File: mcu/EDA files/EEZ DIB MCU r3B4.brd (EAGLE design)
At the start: 139.5 x 70 mm, 201 parts, among them IC1 TPD4E001DRLR, IC10 N.C., IC11 TPS2051BDBVR, IC12 TPS61169DCKR, IC13 TPD4E001DRLR, IC14 TSC2007IPW, IC15 N.C., IC16 DP83848CVV/NOPB, IC2 74AUP1G74DC.125, IC3 CD74HC4050PWR, IC4 STM32F769IIT6, IC5 LD1117ADT33TR, IC6 N.C., IC7 IS42S16400J, IC8 AT24C256C-SSHL-B, IC9 N.C., J1 503398-1892, J2 67803-8020, Q1 N.C., Q2 2N7002, SW1 TL1100CF160Q, SW2 PEC16-2215F-S0024, X1 DS1024-2*20R0, X2 DS1013-16SSIB1, X3 691322110005, X4 N.C., X5 LMJTAB881243M-L, Y1 25MHz, Y2 XTAL016178-85SMX

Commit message: #105
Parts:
- J1: value 503398-1892 -> 5033981892; device EEZ_Lib1:5033981892 -> EEZ_Lib1:5033981892-PCBA
- moved J1 0.60 mm to (49.7, 14.7)
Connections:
- net GND: now also J1.S3
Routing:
- net GND: track 183.0 -> 179.8 mm, vias 320 -> 316
- net LTDC_G6: track 54.6 -> 51.9 mm
- net LTDC_G5: track 31.8 -> 32.3 mm
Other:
- board text added: "EEZ DIB MCU (03/2021 r3B4)"
- board text added: "EEZ DIB MCU (03/2021 r3B4) Project source code: github.com/eez-open/modular-psu"
- board text removed: "EEZ DIB MCU (02/2021 r3B3)"
- board text removed: "EEZ DIB MCU (02/2021 r3B3) Project source code: github.com/eez-open/modular-psu"

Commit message: #88
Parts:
- removed C49: N.C., rcl:C0603
- removed IC10: N.C., EEZ_Lib1:SOT65P210X110-5N
- removed JP7: JP2-NOCUT-0805, EEZ_Lib1:JP2-0805-NOCUT
- added C71: 100n, rcl:C0603
- R12: value N.C. -> 4K7
- moved R12 9.09 mm to (51.4, 65.3), turned to 0 degrees
- moved R4 5.27 mm to (30.1, 11.5)
- moved R8 5.25 mm to (32.7, 11.5)
- moved R22 4.27 mm to (51.4, 67.2)
- moved R25 3.58 mm to (51.4, 63.3)
- moved X3 2.25 mm to (33.8, 6.75)
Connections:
- removed net N$38: R8.2, R9.1
- removed net NRST: IC10.2, IC4.31, JP7.2, R12.2, R25.2
- new net N$60: R4.1, X3.1
- net !RESET: now also C71.2, IC4.31, R12.2, R25.2; no longer IC10.4, JP7.1
- net +3V3: no longer C49.1, IC10.1, IC10.5
- net GND: now also C71.1; no longer C49.2, IC10.3
- net N$41: now also IC1.2, R8.2, R9.1; no longer R4.2, R5.1
- net X_DIN1: now also R4.2, R5.1; no longer R4.1, X3.1
- net X_DIN2: no longer IC1.2
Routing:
- net NRST: track 31.7 -> 0.00 mm
- net !RESET: track 163.5 -> 179.0 mm
- net N$41: track 2.04 -> 9.24 mm, vias 0 -> 2
- net N$60: track 0.00 -> 5.20 mm
- net X_DIN2: track 9.83 -> 4.83 mm, vias 2 -> 0
- net +3V3: track 166.5 -> 163.2 mm, vias 76 -> 75
- net SWD_NRST: track 45.9 -> 48.3 mm
- net N$59: track 5.50 -> 3.18 mm
- net X_DOUT2: track 29.3 -> 31.6 mm
- net X_DOUT1: track 25.9 -> 28.2 mm
- net N$38: track 2.04 -> 0.00 mm
- net X_DIN1: track 12.3 -> 11.7 mm
- net GND: vias 316 -> 315
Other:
- board text added: "EEZ DIB MCU (05/2021 r3B4)"
- board text added: "EEZ DIB MCU (05/2021 r3B4) Project source code: github.com/eez-open/modular-psu"
- board text removed: "EEZ DIB MCU (03/2021 r3B4)"
- board text removed: "EEZ DIB MCU (03/2021 r3B4) Project source code: github.com/eez-open/modular-psu"

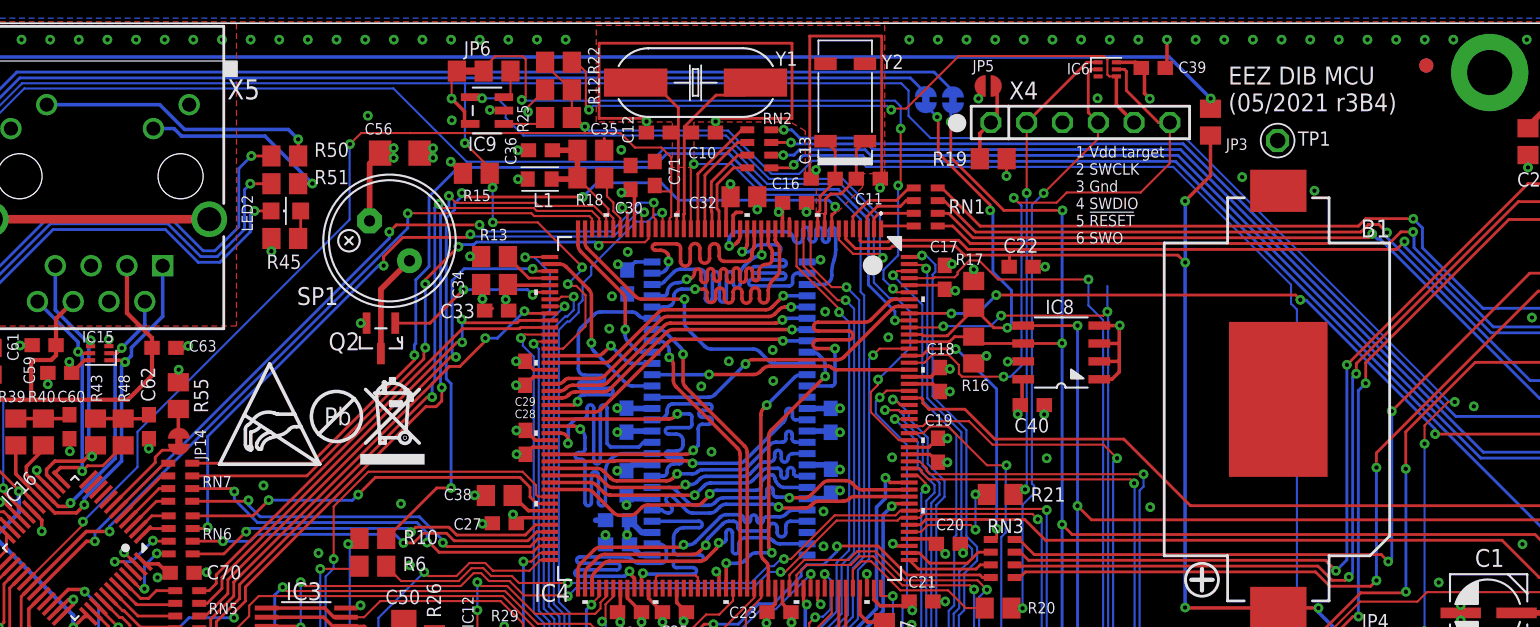
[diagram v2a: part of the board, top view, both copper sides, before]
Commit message: PCB layout for SMD/THT loudspeaker
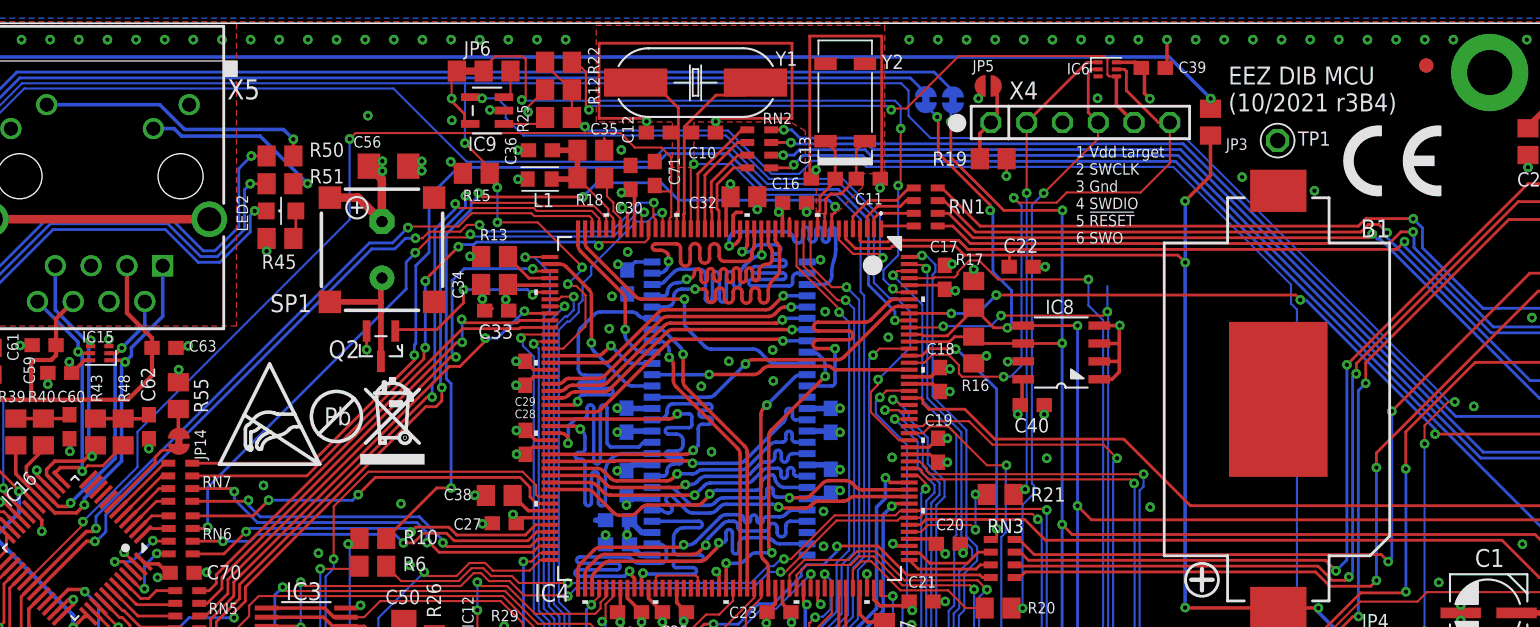
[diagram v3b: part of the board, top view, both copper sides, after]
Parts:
- added U$3: (no value), logo:CE_5MM
- C10, C12: value 33p -> 18p
- SP1: device EEZ_Lib1:LD-BZEN-0903 -> EEZ_Lib1:LD-BZEN_COMBO
- moved C56 1.22 mm to (39.4, 59.9)
- moved SH1 1.04 mm to (38.9, 56.6)
- moved SP1 0.83 mm to (38.9, 53.9), turned to 0 degrees
- moved Q2 0.56 mm to (38.8, 47.1)
- moved LED2 0.34 mm to (31.7, 56.7)
- moved R45 0.34 mm to (31.7, 54.7)
- moved R50 0.34 mm to (31.7, 60.6)
- moved R51 0.34 mm to (31.7, 58.6)
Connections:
- net N$20: now also SP1.+
- net N$5: now also SP1.-
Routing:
- net N$20: track 0.00 -> 4.92 mm
- net N$5: track 7.43 -> 9.58 mm
- net +3V3: track 163.2 -> 161.7 mm
- net ETH_TX_CLK: track 46.9 -> 45.5 mm
- net GND: track 179.8 -> 180.7 mm
- net DAC_OUT1: track 12.2 -> 13.0 mm
- net ETH_RX_CLK: track 55.4 -> 54.7 mm
- net ETH_CRS: track 63.4 -> 62.7 mm
- net DIN2: track 57.0 -> 56.3 mm
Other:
- board text added: "EEZ DIB MCU (10/2021 r3B4)"
- board text added: "EEZ DIB MCU (10/2021 r3B4) Project source code: github.com/eez-open/modular-psu"
- board text removed: "EEZ DIB MCU (05/2021 r3B4)"
- board text removed: "EEZ DIB MCU (05/2021 r3B4) Project source code: github.com/eez-open/modular-psu"
